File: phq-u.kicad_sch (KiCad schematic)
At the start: 48 parts, among them J1 18…56 V, J2 MCU bypass, J3 Voltage select, J4 3.3…24 V, Q1 NX138AK, U1 i7A4W033A033V, U2 TMCS1108A1U, U3 TMCS1108A1U

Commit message: Exclude optional ground bias resistor from BOM
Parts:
- R14: now left out of the parts list
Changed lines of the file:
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@@
   )
   (symbol (lib_id "Device:R_Small") (at 266.7 87.63 0) (unit 1)
-    (in_bom yes) (on_board yes) (fields_autoplaced)
+    (in_bom no) (on_board yes) (fields_autoplaced)
     (property "Reference" "R14" (id 0) (at 268.1986 86.7215 0)
       (effects (font (size 1.27 1.27)) (justify left))

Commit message: Add 3.3 V TVS diodes and revise ground zones
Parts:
- added D? (x2): 3V3, Diode_SMD:D_0402_1005Metric, symbol Device:D_Zener_Small
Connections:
- net +3V3: now also D?.1 (K), D?.1 (K)
- net GNDD: now also D?.2 (A), D?.2 (A)
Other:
- moved on the sheet: C4, C5

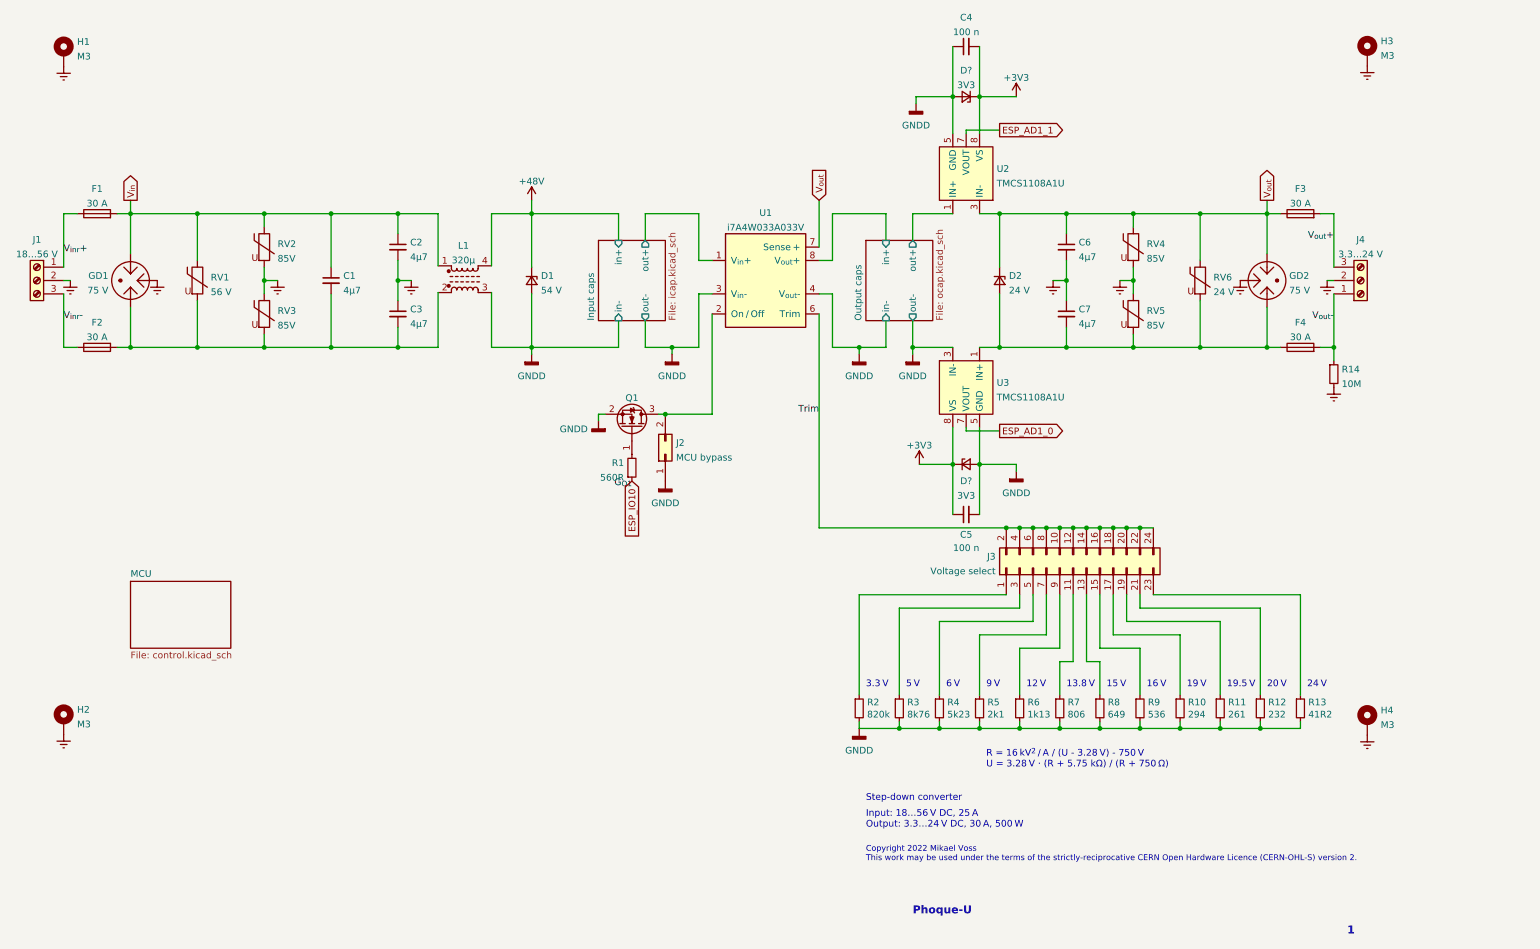
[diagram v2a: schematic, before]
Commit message: Clean up schematic
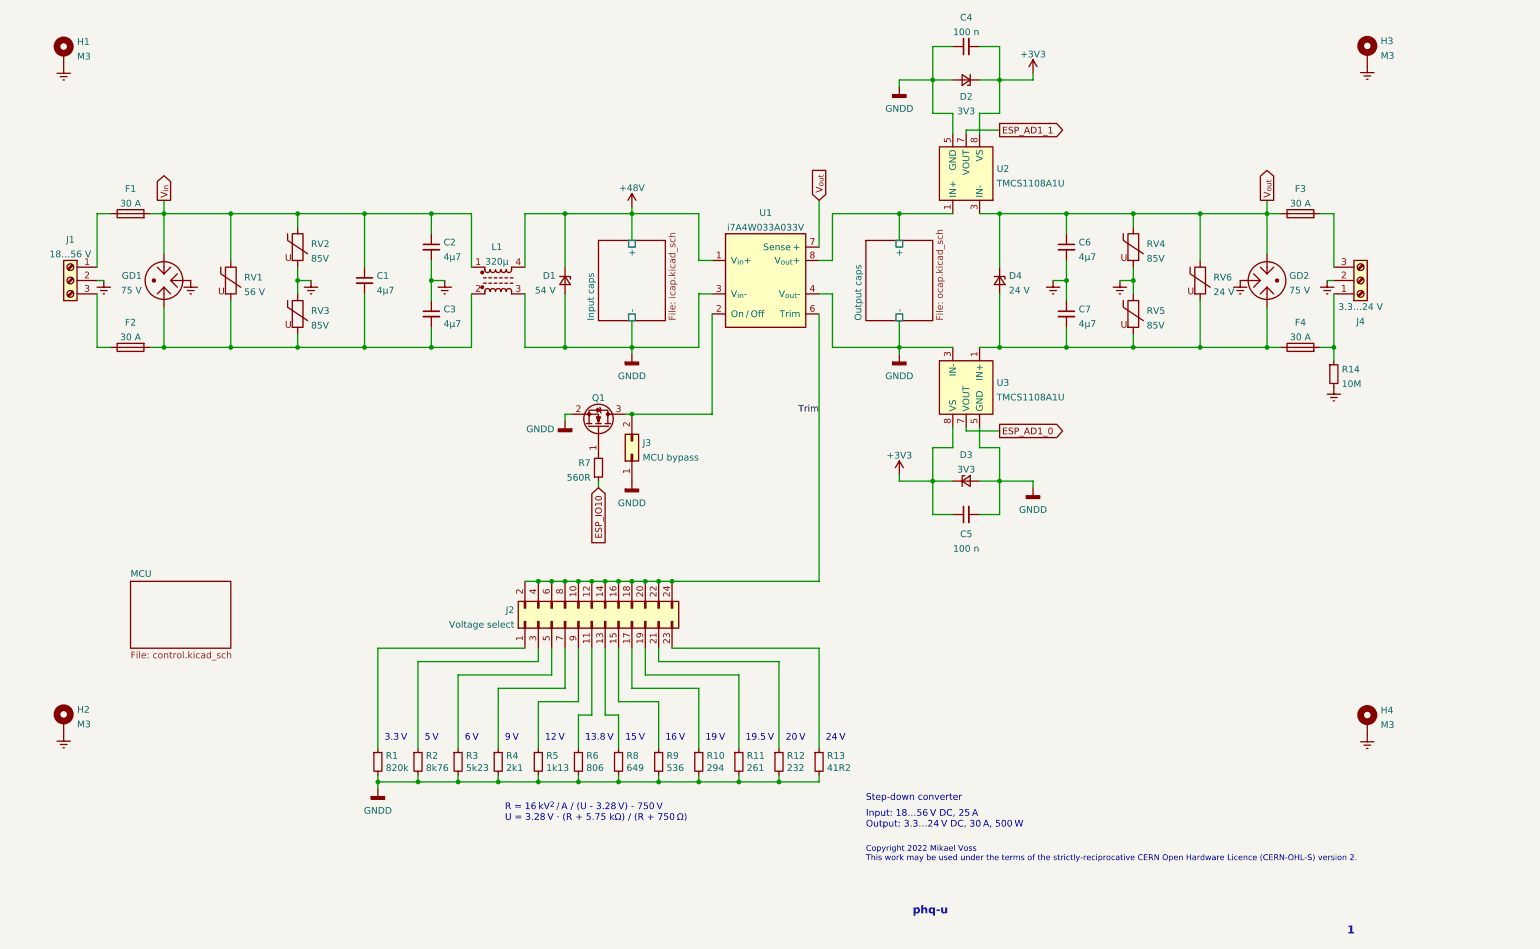
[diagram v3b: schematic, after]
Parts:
- gave numbers to parts that had none: 2
- renumbered D2 to D4, J3 to J2, J2 to J3, R2 to R1, R3 to R2, R4 to R3, R5 to R4, R6 to R5, R7 to R6, R1 to R7
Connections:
- net Input caps/out+ is gone; now on net +48V: U1.1 (V_{in}+)
- net Output caps/out+ is gone; now on net Output caps/+: U2.1 (IN+), U2.2 (IN+)
- net Output caps/in+ renamed Output caps/+
- net V_{inr}+: no longer names the net of F1.1, J1.1 (Pin_1)
- net V_{inr}-: no longer names the net of F2.1, J1.3 (Pin_3)
- net V_{out}+: no longer names the net of F3.2, J4.3 (Pin_3)
- net V_{out}-: no longer names the net of F4.2, J4.1 (Pin_1), R14.1
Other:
- sheet Input caps ports: added +, -; removed in+, in-, out+, out-
- sheet Output caps ports: added +, -; removed in+, in-, out+, out-
- note added: "phq-u"
- note removed: "Phoque-U"
- moved on the sheet: C1, C2, C3, D1, D2, D3, F1, F2, GD1, J1, J2, J3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

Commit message: Replace resistors with available variants
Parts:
- C2, C3: Manufacturer (none) -> Kyocera AVX; Part Number CD45-E2GA472M-NKA -> 12101C475K4T2A
- D4: Part Number SMA6F24A -> SMA6F24A
- Q1: value NX138AK -> NX138AKR; Part Number NX138AK -> NX138AKR
- R10: value 294 -> 287
- R2: value 8k76 -> 8k66
- R7: footprint Resistor_SMD:R_0603_1608Metric -> Resistor_SMD:R_0402_1005Metric
- RV2, RV3, RV4, RV5: Part Number ZV60K1206121NIR1 -> ZV60K1206121NIR1
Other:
- note added: "R = 16.4 kV^{2} / A / (U - 3.28 V) - 750 V U = 3.28 V · (R + 5.75 kΩ) / (R + 750 Ω)"
- note removed: "R = 16 kV^{2} / A / (U - 3.28 V) - 750 V U = 3.28 V · (R + 5.75 kΩ) / (R + 750 Ω)"

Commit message: Add separate ADCs for remote measurements
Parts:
- F1, F2: value 30 A -> 20 A
- J2: value Voltage select -> Output voltage
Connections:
- net ESP_AD1_0 renamed I_{-}
- net ESP_AD1_1 renamed I_{+}
- net ESP_IO10 renamed DC_EN

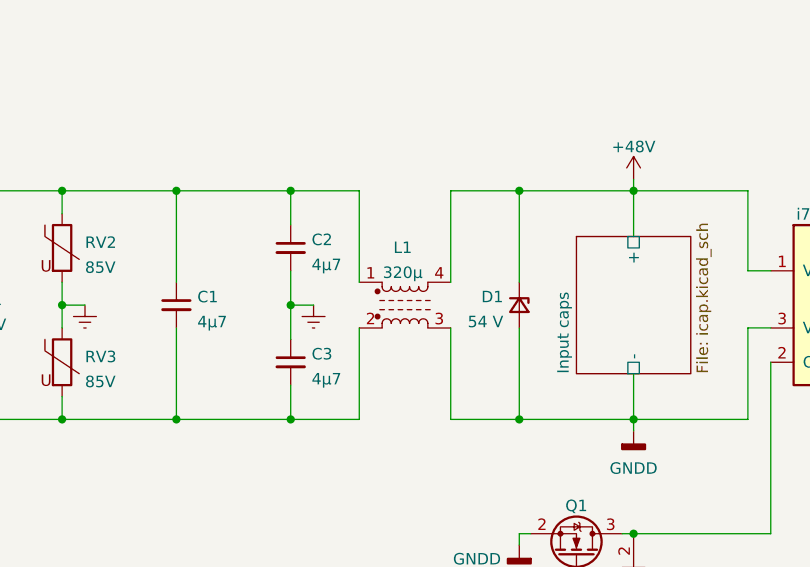
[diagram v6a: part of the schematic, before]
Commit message: Replace common‐mode choke
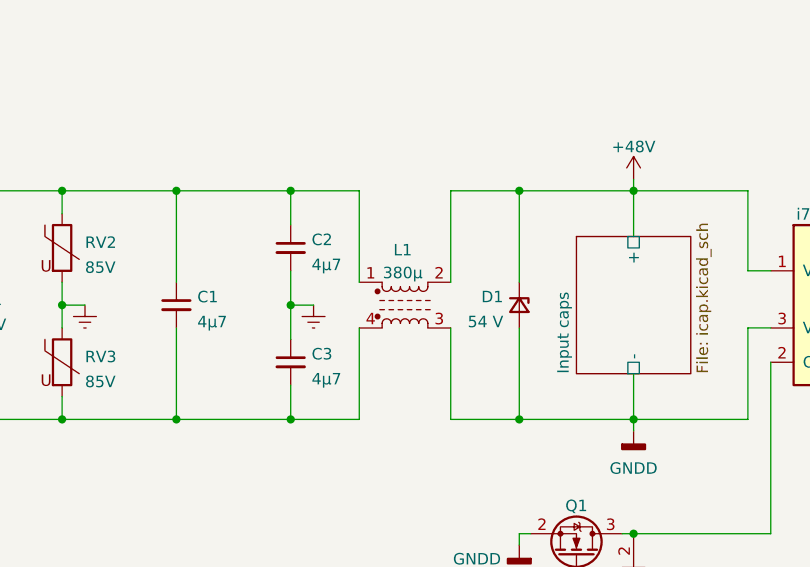
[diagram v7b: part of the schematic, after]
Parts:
- L1: value 320µ -> 380µ; footprint phq_SMD:CMX1211Z321B-10 -> phq_SMD:B82722S0; symbol Device:L_Ferrite_Coupled_1423 -> Device:L_Ferrite_Coupled_1243; Manufacturer (none) -> TDK; Part Number (none) -> B82722S0193A040
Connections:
- net +48V: now also L1.2; no longer L1.4
- net at C1.2, C3.2, F2.2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: now also L1.4; no longer L1.2
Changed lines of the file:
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@@
     (pin "1")
   )
-  (symbol (lib_id "Device:L_Ferrite_Coupled_1423") (at 107.95 69.85 0) (unit 1)
-    (in_bom yes) (on_board yes) (fields_autoplaced)
-    (property "Reference" "L1" (id 0) (at 107.696 63.4705 0))
-    (property "Value" "320µ" (id 1) (at 107.696 66.2456 0))
-    (property "Footprint" "phq_SMD:CMX1211Z321B-10" (id 2) (at 107.95 69.85 0)
+  (symbol (lib_id "Device:L_Ferrite_Coupled_1243") (at 107.95 69.85 0) (unit 1)
+    (in_bom yes) (on_board yes) (fields_autoplaced)
+    (property "Reference" "L1" (id 0) (at 107.696 63.7372 0))
+    (property "Value" "380µ" (id 1) (at 107.696 66.2741 0))
+    (property "Footprint" "phq_SMD:B82722S0" (id 2) (at 107.95 69.85 0)
       (effects (font (size 1.27 1.27)) hide)
     )
     (property "Datasheet" "~" (id 3) (at 107.95 69.85 0)
+      (effects (font (size 1.27 1.27)) hide)
+    )
+    (property "Manufacturer" "TDK" (id 4) (at 107.95 69.85 0)
+      (effects (font (size 1.27 1.27)) hide)
+    )
+    (property "Part Number" "B82722S0193A040" (id 5) (at 107.95 69.85 0)
       (effects (font (size 1.27 1.27)) hide)
     )
@@
     )
     (path "/d80a4652-e7ed-4566-92f6-76a18cabb7d6"
-      (reference "L1") (unit 1) (value "320µ") (footprint "phq_SMD:CMX1211Z321B-10")
+      (reference "L1") (unit 1) (value "380µ") (footprint "phq_SMD:B82722S0")
     )
     (path "/b964d121-1ca9-4d94-9cd9-a72a5247427a/cb7151d5-e2ab-4025-b1e2-8bdcd9fdf752"

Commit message: Add 100 nF bypass capacitor to ESP32 power input
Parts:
- D1: Part Number 1.5SMBJ54A-H -> 1.5SMBJ54A-H
